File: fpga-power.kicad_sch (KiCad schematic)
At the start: 76 parts, among them U15 XC7K160T-FFG676

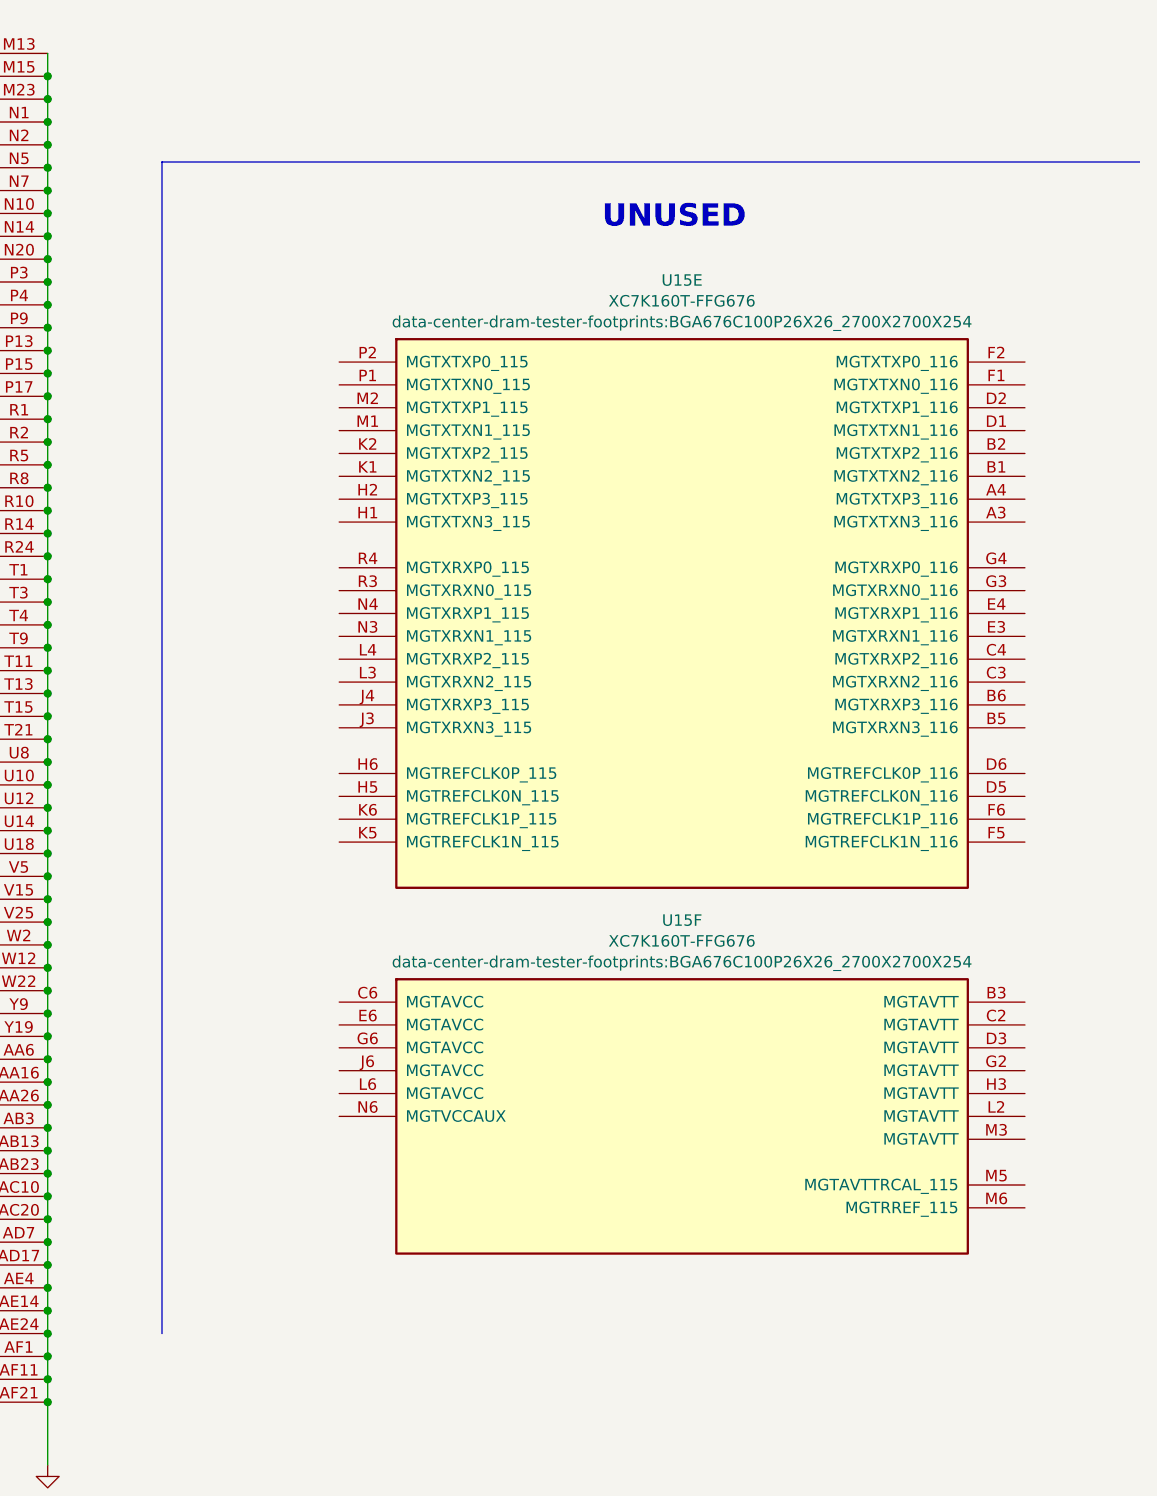
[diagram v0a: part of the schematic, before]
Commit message: Added PCIe sheet, initial connection of the PCIe interface
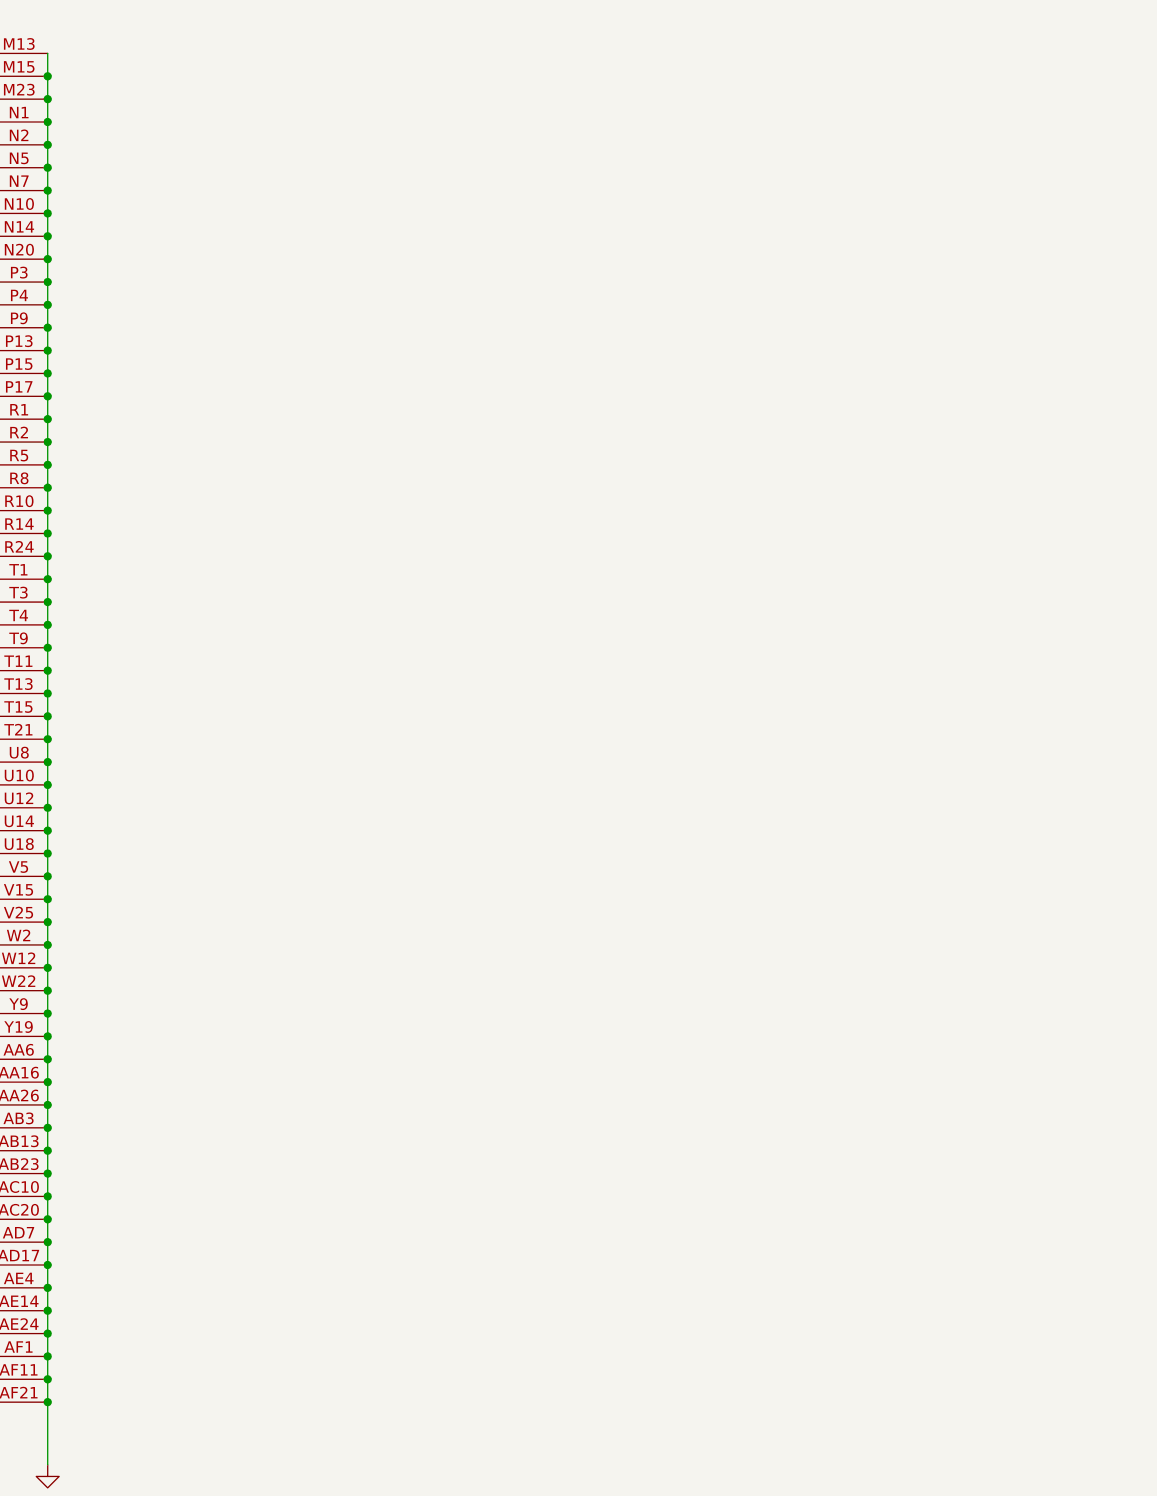
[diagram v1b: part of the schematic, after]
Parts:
- removed unit 5 of U15
- removed unit 6 of U15
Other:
- note removed: "UNUSED"

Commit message: Update FPGA symbol (die to pad length), initial fanout for die [1..4]
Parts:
- U15: footprint data-center-dram-tester-footprints:BGA676C100P26X26_2700X2700X254 -> antmicro-footprints:xc7k160tfbg676
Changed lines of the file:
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@@
     (property "Reference" "U15" (id 0) (at 261.62 53.7972 0))
     (property "Value" "XC7K160T-FFG676" (id 1) (at 261.62 56.1086 0))
-    (property "Footprint" "data-center-dram-tester-footprints:BGA676C100P26X26_2700X2700X254" (id 2) (at 261.62 58.42 0)
+    (property "Footprint" "antmicro-footprints:xc7k160tfbg676" (id 2) (at 261.62 58.42 0)
       (effects (font (size 1.27 1.27)) hide)
     )

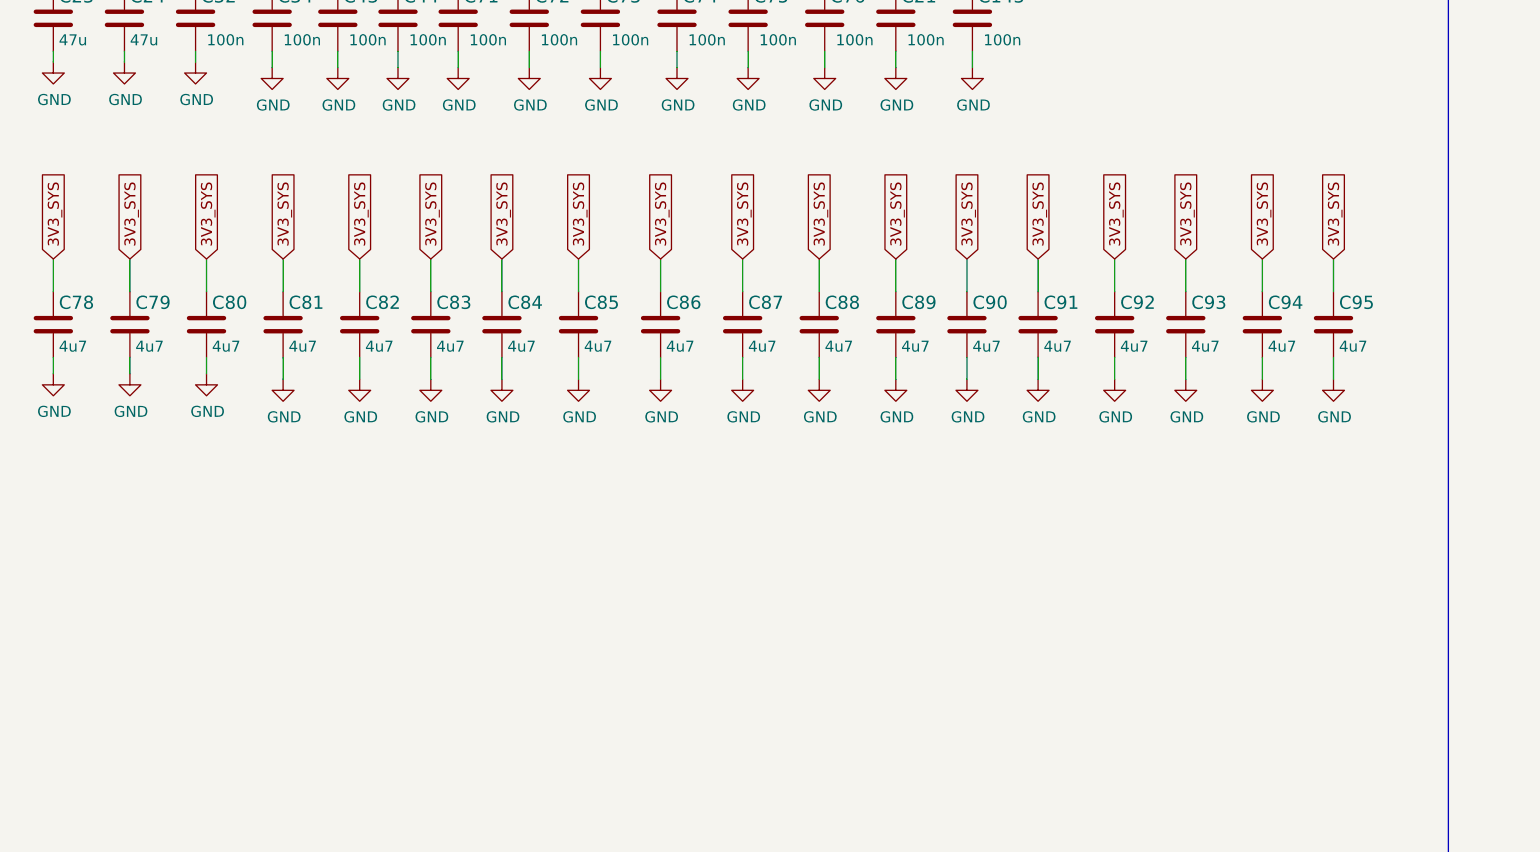
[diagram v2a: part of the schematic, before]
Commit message: Route internal end external (FMC) ETH interface, add additional VDDQ and ETH MUX decoupling
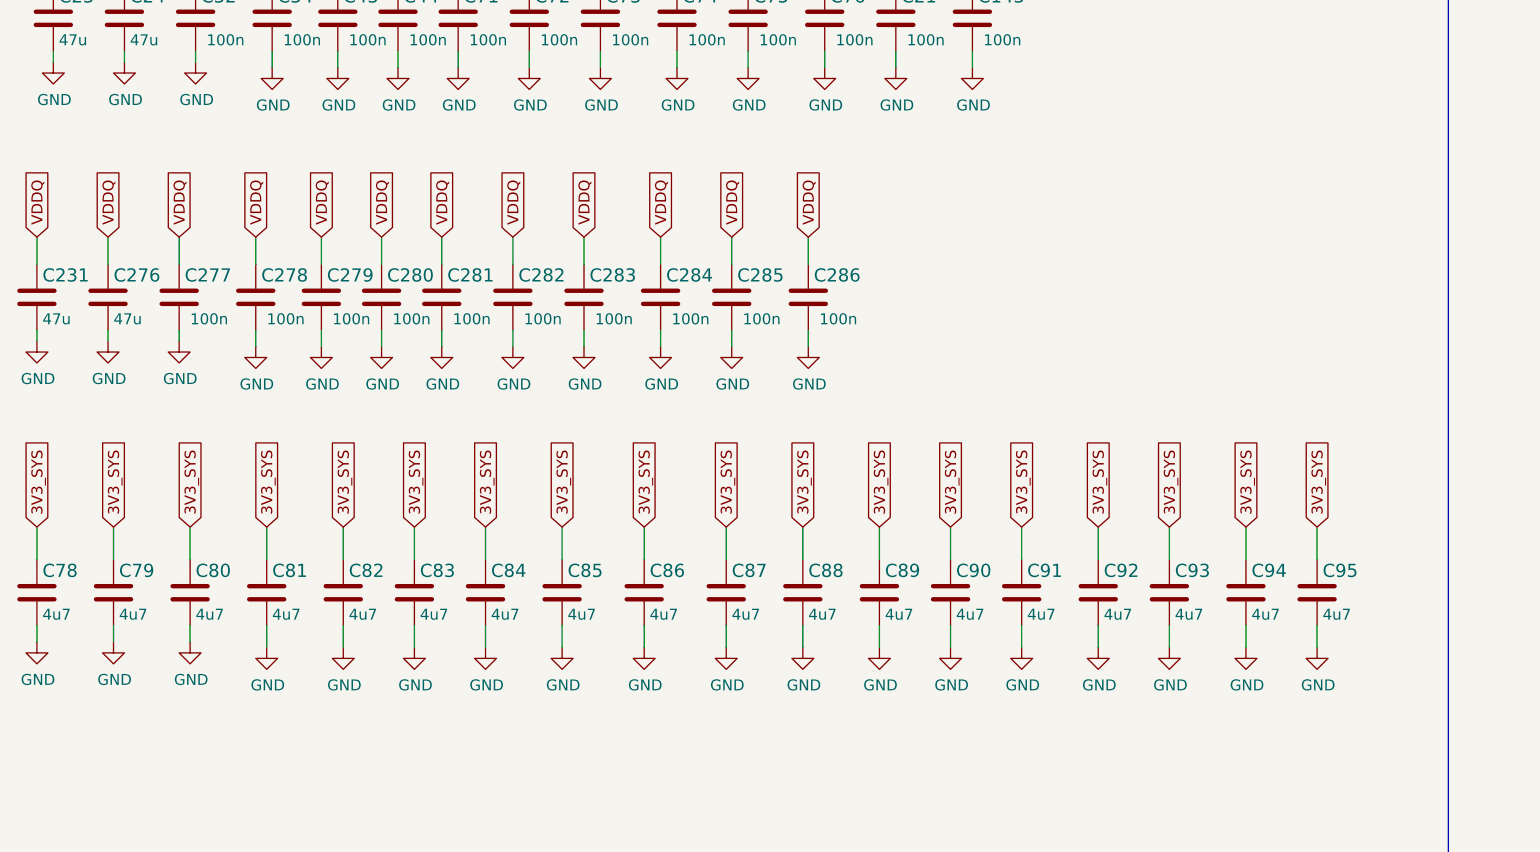
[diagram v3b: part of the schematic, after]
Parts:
- added C231, C276: C_47u_0603, data-center-dram-tester-footprints:0603-cap, symbol data-center-dram-tester:C_47u_0603
- added C277, C278, C279, C280, C281, C282, C283, C284, C285, C286: C_100n_0201, data-center-dram-tester-footprints:0201-res, symbol data-center-dram-tester:C_100n_0201
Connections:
- net GND: now also C231.2, C276.2, C277.2, C278.2, C279.2, C280.2, C281.2, C282.2, C283.2, C284.2, C285.2, C286.2
- net VDDQ: now also C231.1, C276.1, C277.1, C278.1, C279.1, C280.1, C281.1, C282.1, C283.1, C284.1, C285.1, C286.1
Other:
- moved on the sheet: C78, C79, C80, C81, C82, C83, C84, C85, C86, C87, C88, C89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

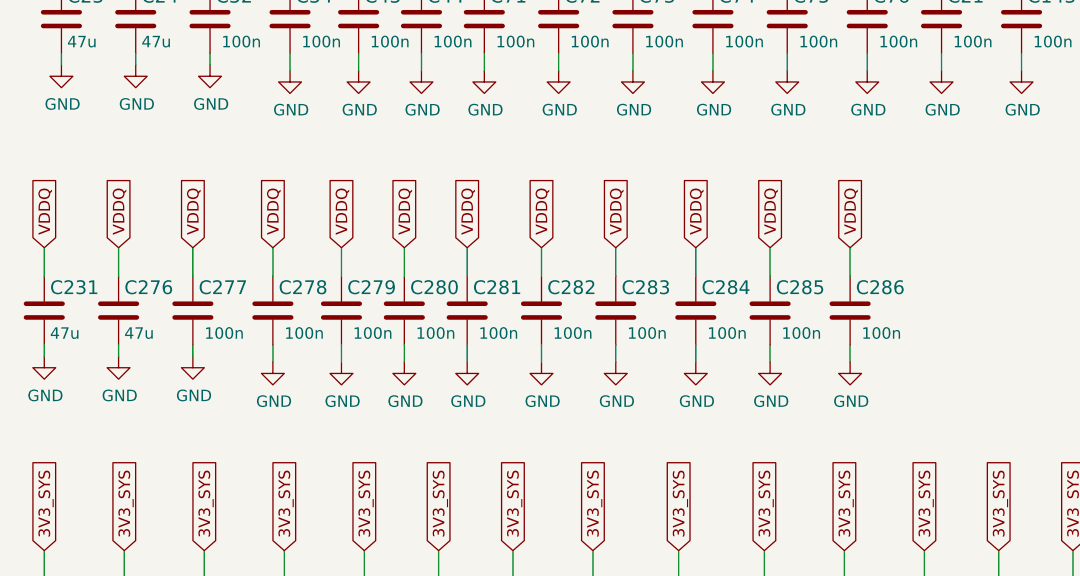
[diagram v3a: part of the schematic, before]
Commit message: Add ETH MUX passthrough, reroute HDMI to 100 Ohm differential, begin routing current measurment circuit
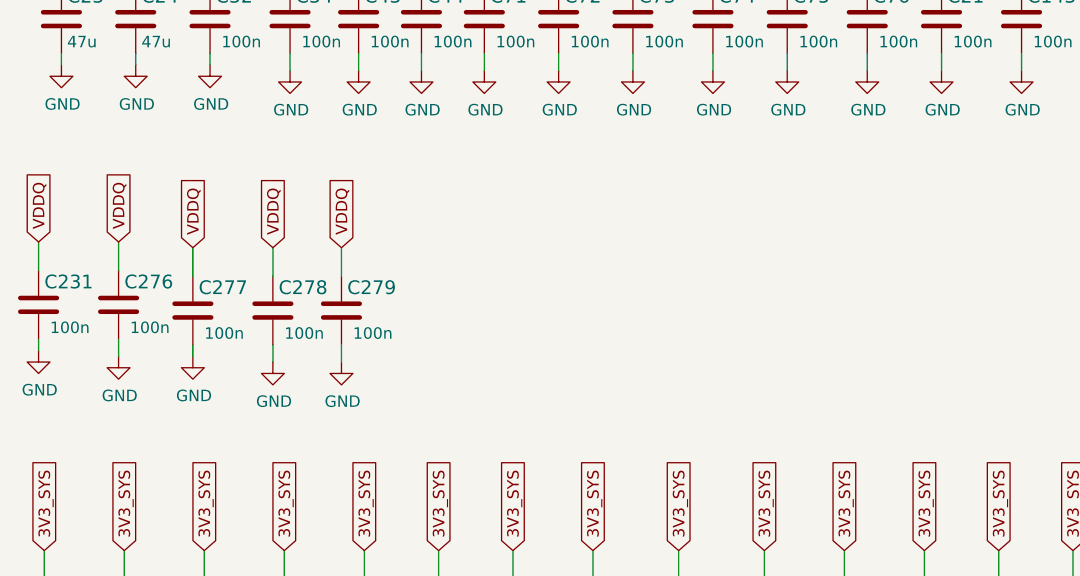
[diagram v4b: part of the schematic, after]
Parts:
- removed C231, C276: C_47u_0603, data-center-dram-tester-footprints:0603-cap, symbol data-center-dram-tester:C_47u_0603
- removed C280, C281, C282, C283, C284, C285, C286: C_100n_0201, data-center-dram-tester-footprints:0201-res, symbol data-center-dram-tester:C_100n_0201
- added C231, C276: C_100n_0201, data-center-dram-tester-footprints:0201-res, symbol data-center-dram-tester:C_100n_0201
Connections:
- net GND: now also C231.2, C276.2
- net VDDQ: now also C231.1, C276.1

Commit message: Cleanup schematic
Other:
- moved on the sheet: C11, C114, C115, C14, C143, C144, C16, C17, C19, C20, C21, C22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
